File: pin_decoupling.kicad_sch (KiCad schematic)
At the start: 108 parts, among them Q1 RFD14N05L, Q10 RFD14N05L, Q11 RFD14N05L, Q12 RFD14N05L, Q13 RFD14N05L, Q14 RFD14N05L, Q15 RFD14N05L, Q16 RFD14N05L, Q17 RFD14N05L, Q18 RFD14N05L, Q19 RFD14N05L, Q2 RFD14N05L, Q20 RFD14N05L, Q21 RFD14N05L, Q22 RFD14N05L, Q23 RFD14N05L, Q24 RFD14N05L, Q25 RFD14N05L, Q26 RFD14N05L, Q27 RFD14N05L, Q28 RFD14N05L, Q29 RFD14N05L, Q3 RFD14N05L, Q30 RFD14N05L, Q31 RFD14N05L, Q32 RFD14N05L, Q33 RFD14N05L, Q34 RFD14N05L, Q35 RFD14N05L, Q36 RFD14N05L, Q37 RFD14N05L, Q38 RFD14N05L, Q39 RFD14N05L, Q4 RFD14N05L, Q40 RFD14N05L, Q41 RFD14N05L, Q42 RFD14N05L, Q43 RFD14N05L, Q44 RFD14N05L, Q45 RFD14N05L, Q46 RFD14N05L, Q47 RFD14N05L, Q48 RFD14N05L, Q5 RFD14N05L, Q6 RFD14N05L, Q7 RFD14N05L, Q8 RFD14N05L, Q9 RFD14N05L, U2 74HCTLS259, U4 74HCTLS259, U5 74HCTLS259, U6 74HCTLS259, U7 74HCTLS259, U8 74HCTLS259

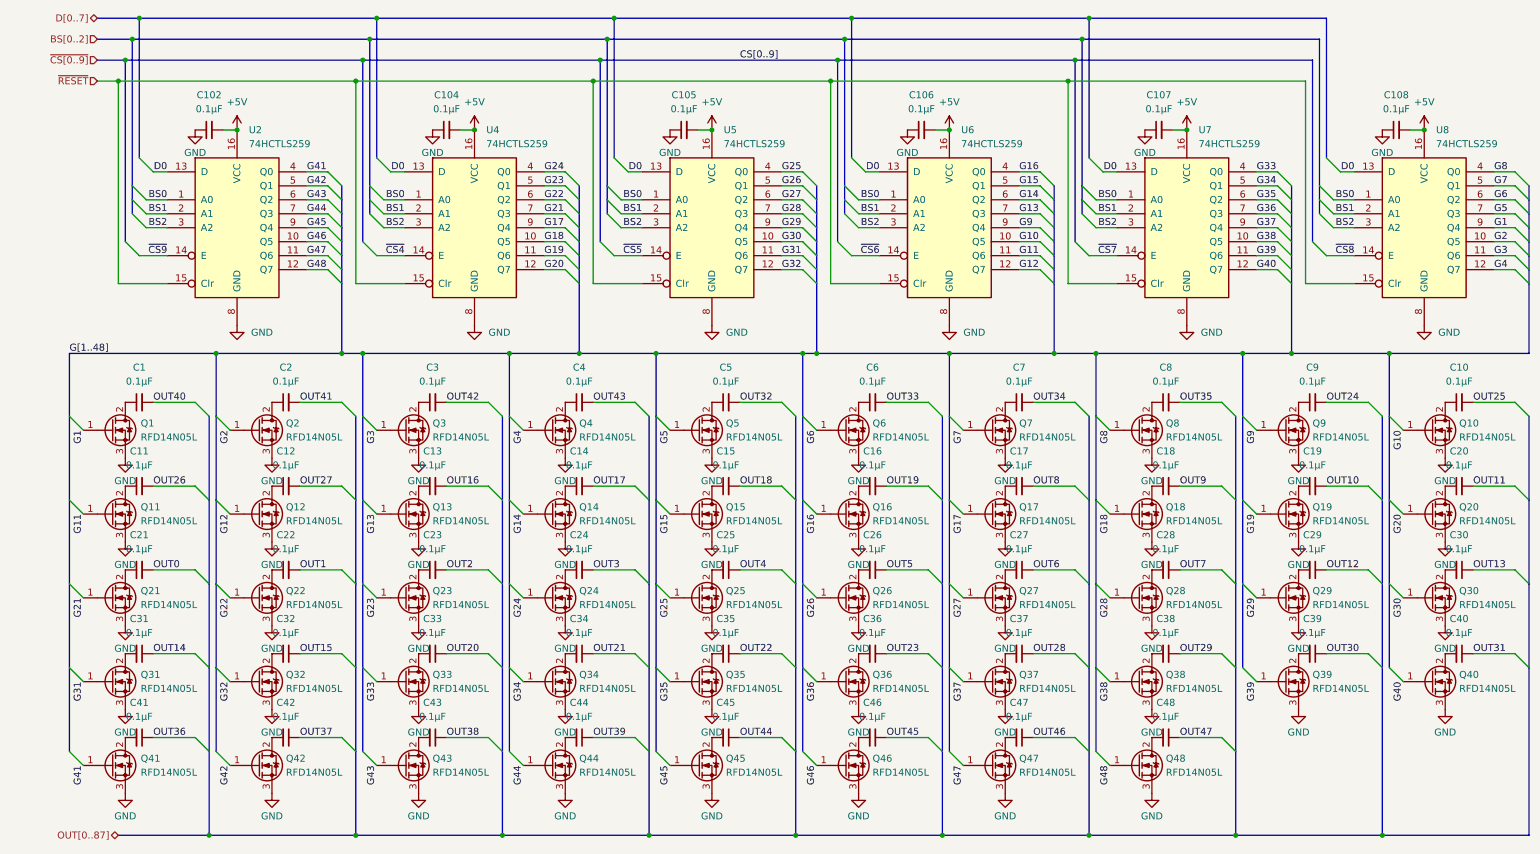
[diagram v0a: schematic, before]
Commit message: updates:
- update symbols and footprints from library
- re-correct 84 pin PLCC pin numbers
- reset transistors to TO-2whatever from SMD
- adjust position of DIN connectors, LEDs and their resistors (and 48 pin DIP and transistors and decoupling capacitors):  measured again.
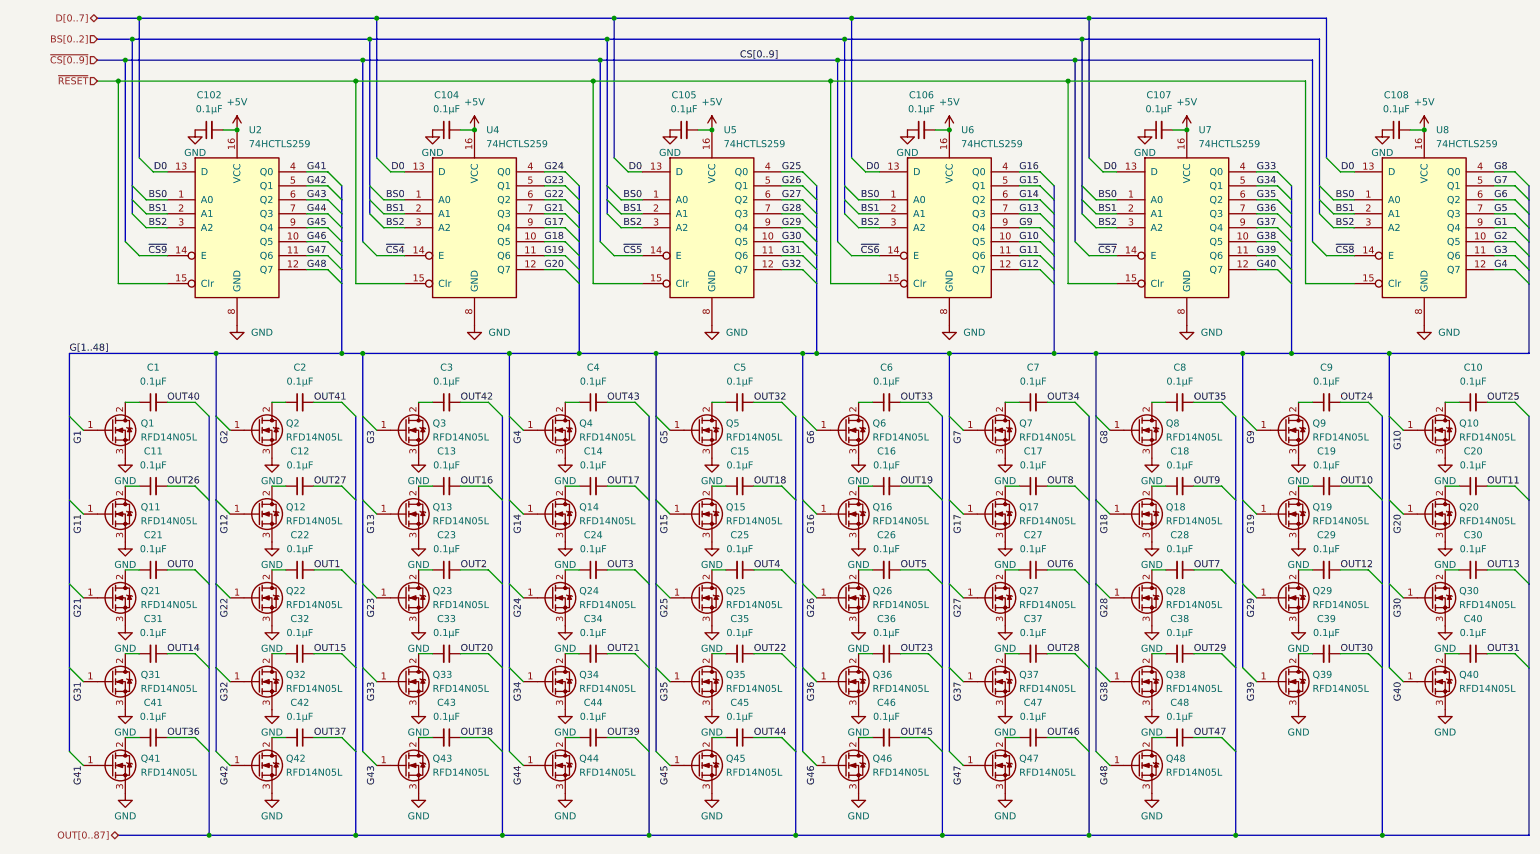
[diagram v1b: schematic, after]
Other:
- moved on the sheet: C1, C10, C11, C12, C13, C14, C15, C16, C17, C18, C19, C2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

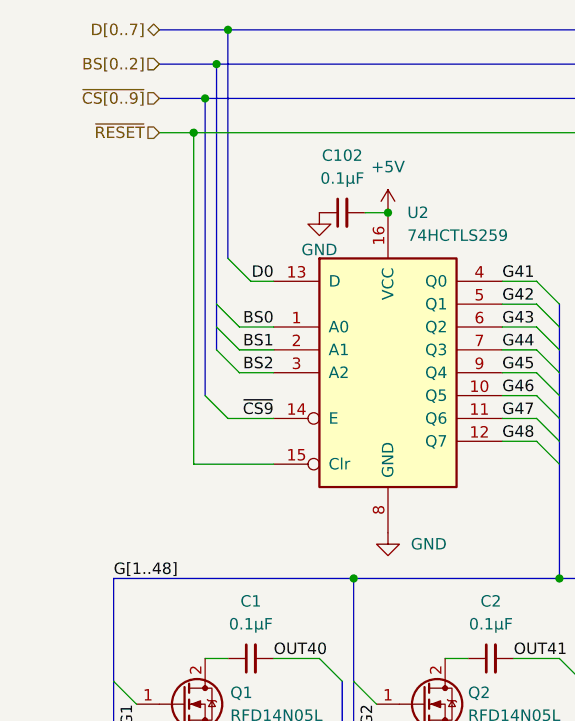
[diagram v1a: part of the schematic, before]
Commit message: decoded PAL contents, added notes
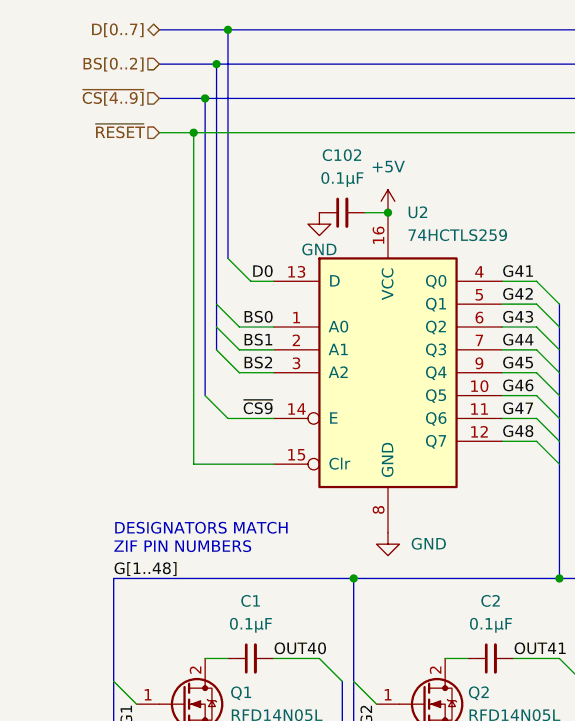
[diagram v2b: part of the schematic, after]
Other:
- note added: "DESIGNATORS MATCH ZIF PIN NUMBERS"
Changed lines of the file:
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@@
 		(title "ALLPRO88 Socket Module Template")
 	)
+	(text "DESIGNATORS MATCH\nZIF PIN NUMBERS"
+		(exclude_from_sim no)
+		(at 17.78 70.612 0)
+		(effects
+			(font
+				(size 1.27 1.27)
+			)
+			(justify left)
+		)
+	)
 	(junction
 		(at 153.67 74.93)
@@
 		)
 	)
-	(hierarchical_label "~{CS[0..9]}"
+	(hierarchical_label "~{CS[4..9]}"
 		(shape input)
 		(at 22.86 21.59 180)
